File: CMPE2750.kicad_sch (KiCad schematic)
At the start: 46 parts, among them J10 Conn_01x16, J5 Conn_02x07_Odd_Even, J6 SPI3, J7 Conn_02x16_Top_Bottom, J8 Conn_01x04, SW3 D6R90F1LFS, U1 STM32L476RGTx, X1 ABS25-32.768KHZ-6-T

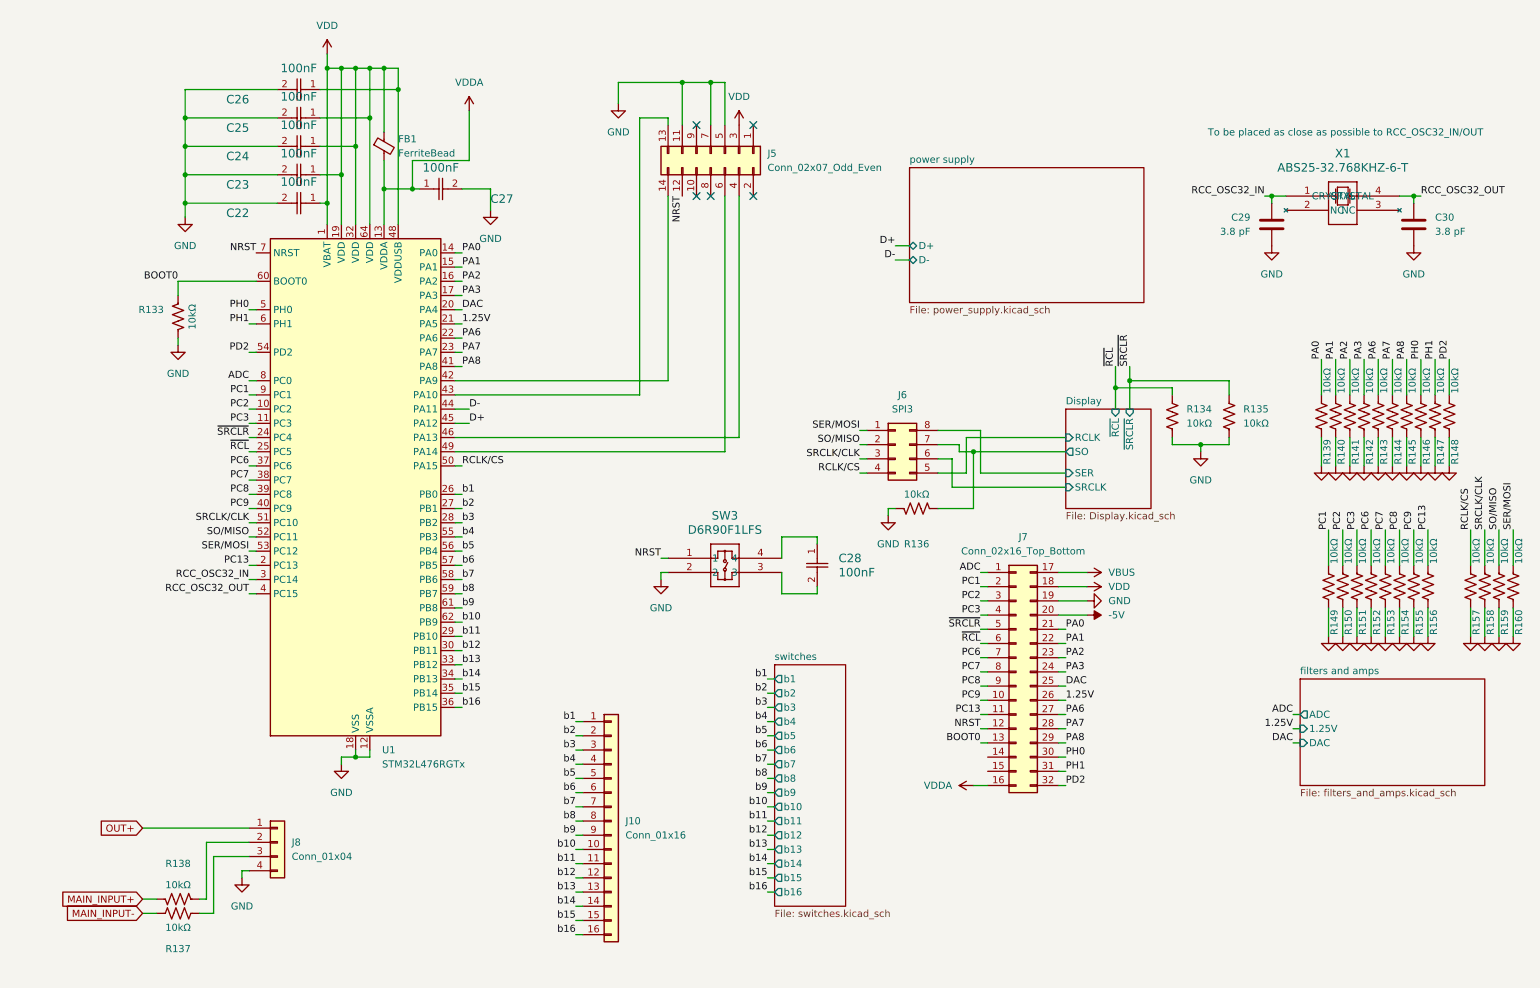
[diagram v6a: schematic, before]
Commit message: Added mounting holes to the schematic, reset the annotations, updated a few footprints, and fixed some issues that were discovered on the ERC.
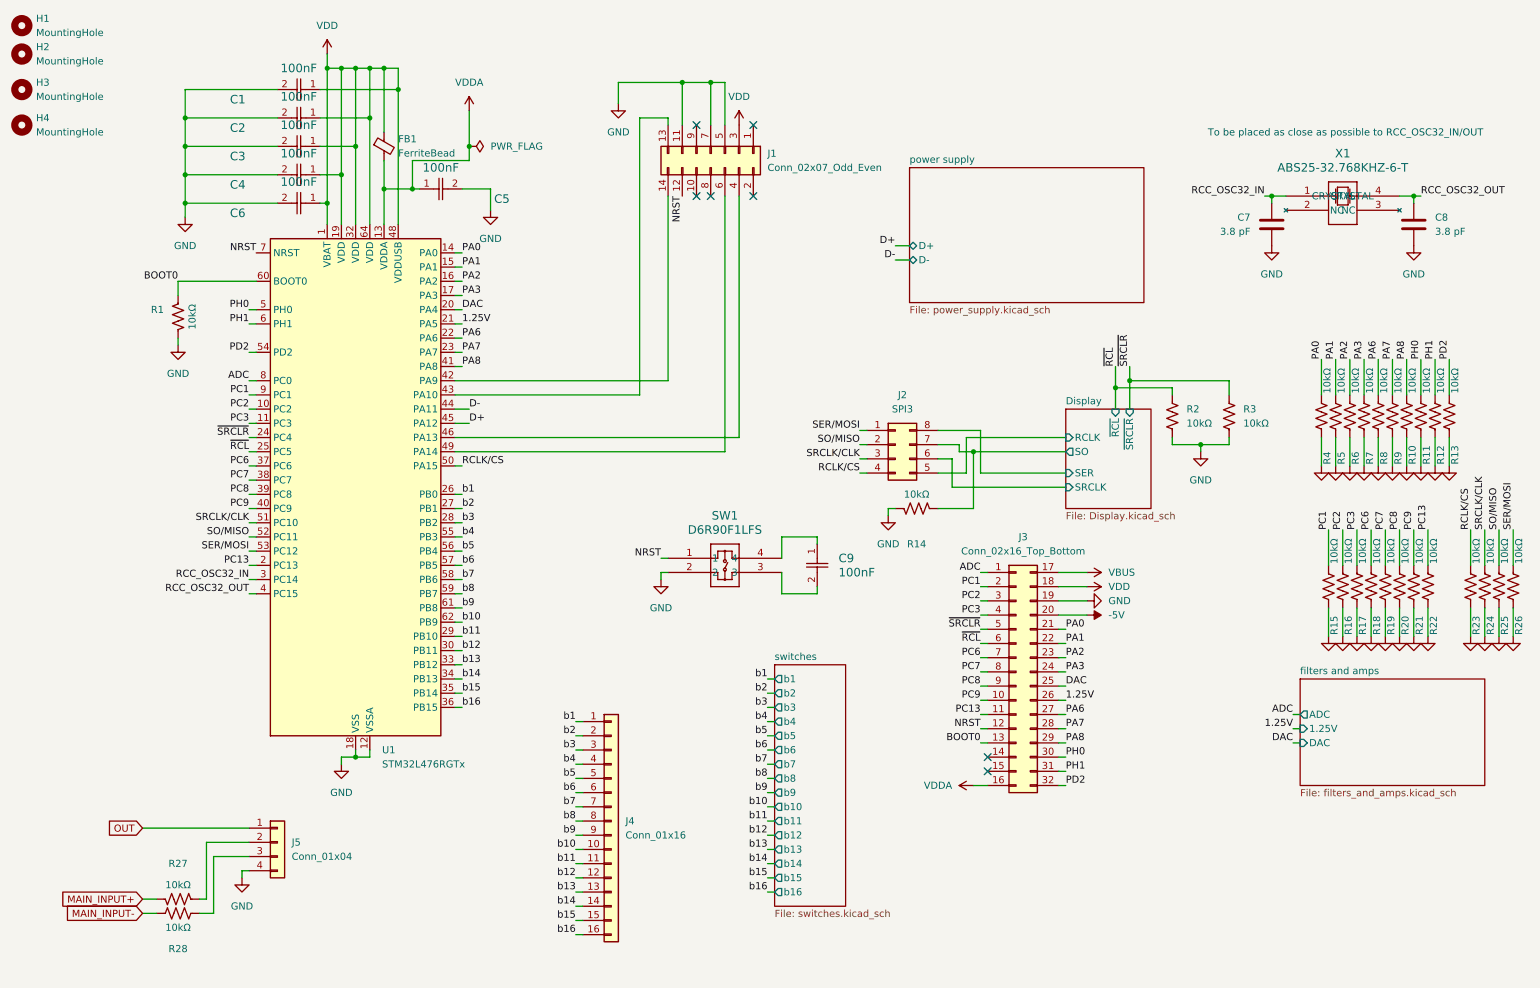
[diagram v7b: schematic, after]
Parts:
- added H1, H2, H3, H4: MountingHole, MountingHole:MountingHole_3.2mm_M3, symbol Mechanical:MountingHole
- SW1: renamed from SW3; footprint D6R_CNK -> CMPE2750:D6R_CNK
- X1: footprint X_ABS25_ABR -> CMPE2750:X_ABS25_ABR
- renumbered C26 to C1, C25 to C2, C24 to C3, C23 to C4, C27 to C5, C22 to C6, C29 to C7, C30 to C8, C28 to C9, J5 to J1, J6 to J2, J7 to J3, J10 to J4, J8 to J5, R133 to R1, R145 to R10, R146 to R11, R147 to R12, R148 to R13, R136 to R14, R149 to R15, R150 to R16, R151 to R17, R152 to R18, R153 to R19, R134 to R2, R154 to R20, R155 to R21, R156 to R22, R157 to R23, R158 to R24, R159 to R25, R160 to R26, R138 to R27, R137 to R28, R135 to R3, R139 to R4, R140 to R5, R141 to R6, R142 to R7, R143 to R8, R144 to R9
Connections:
- net OUT+ renamed OUT
- no-connect marks 5 -> 7

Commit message: Added a ferrite bead and removed a decoupling cap from another ferrite bead
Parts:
- removed C5: 100nF, Capacitor_SMD:C_0402_1005Metric, symbol CMPE2750:CL05B104KP5NNNC
- added FB2: FerriteBead, Inductor_SMD:L_0603_1608Metric, symbol Device:FerriteBead_Small
- renumbered C6 to C5, C7 to C6, C8 to C7, C9 to C8
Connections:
- net GND: now also FB2.2; no longer J5.4 (Pin_4)
- new net: FB2.1, J5.4 (Pin_4)
